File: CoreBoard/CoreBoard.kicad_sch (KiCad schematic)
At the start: 6 parts, among them J1 RJ45_LED_Shielded, U1 OKI, U2 Teensy4.1_DEV-16771

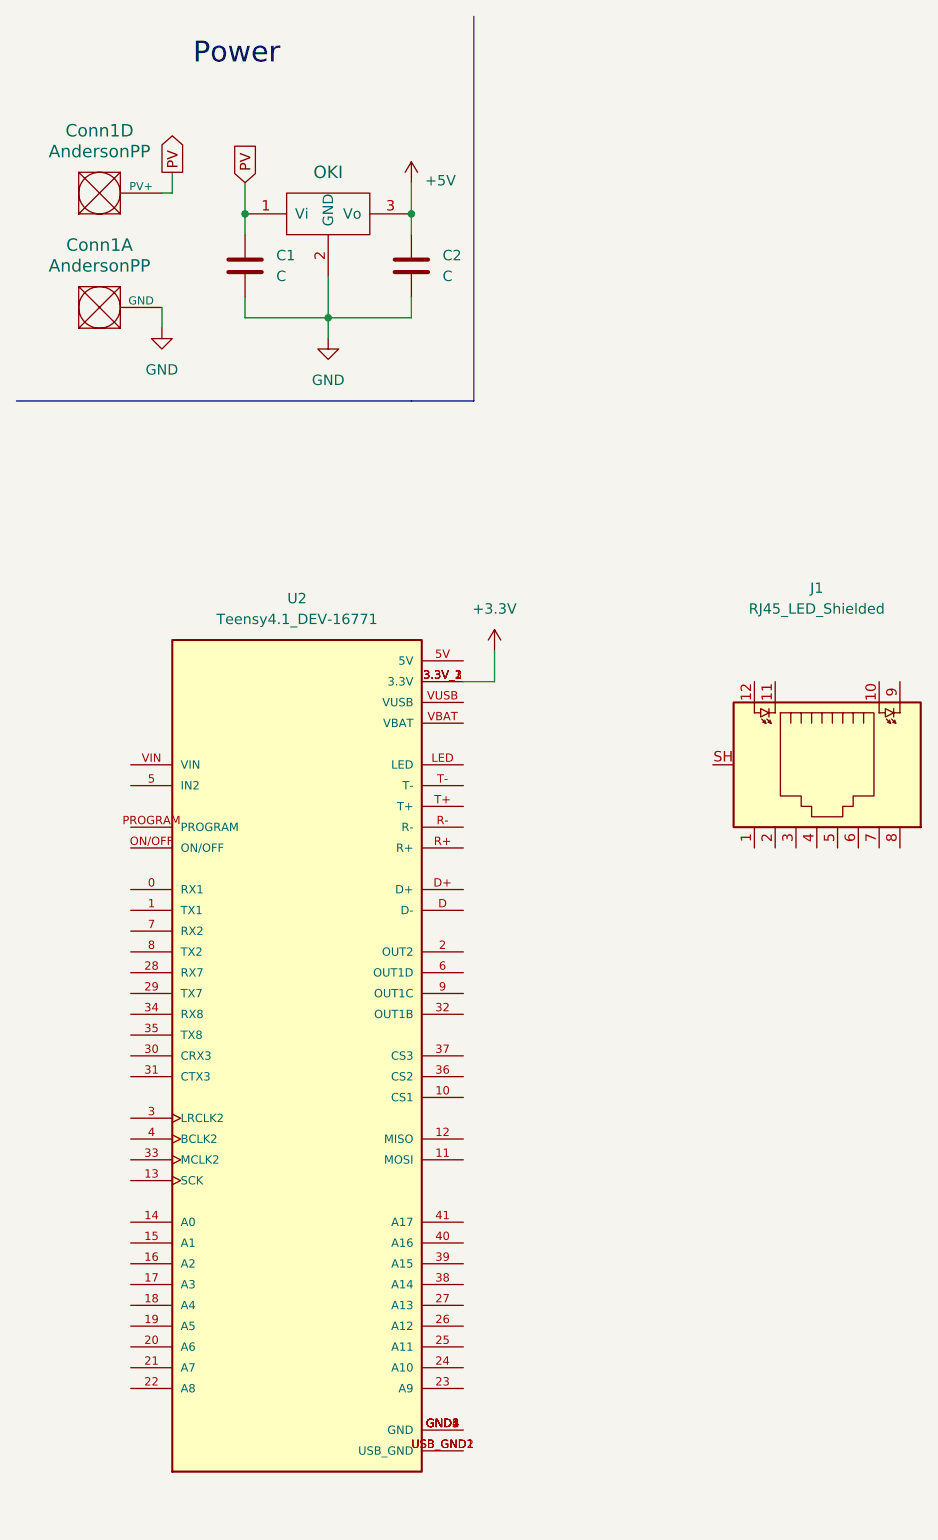
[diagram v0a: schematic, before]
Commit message: Added connections between the Teensy and the Ethernet Port, and the capacitance values were added for capacitors
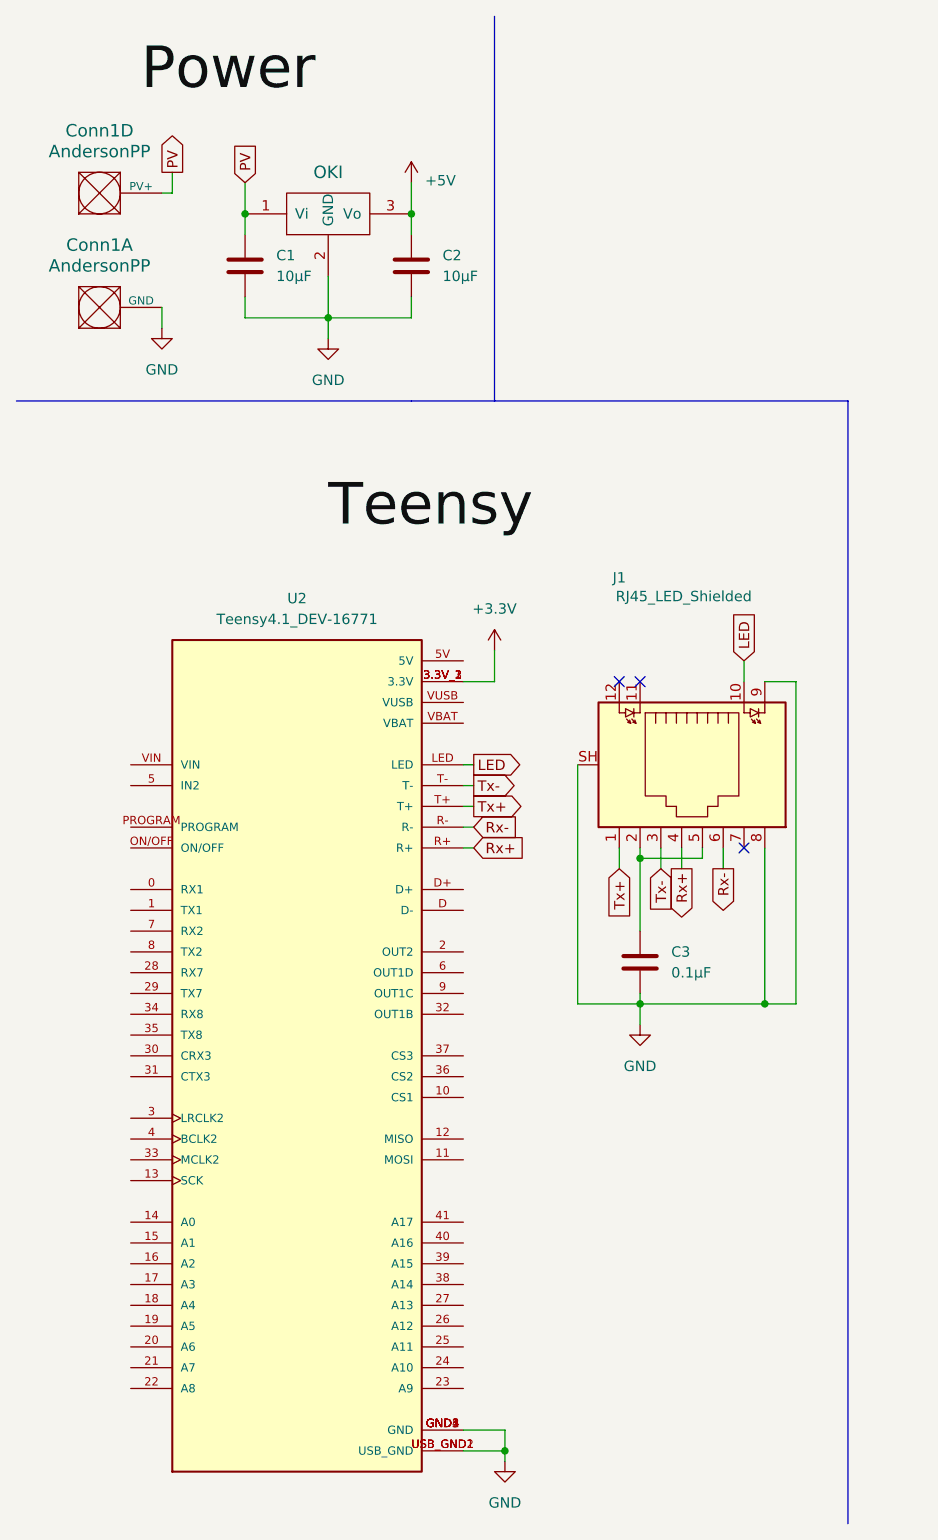
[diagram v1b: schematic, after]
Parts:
- added C3: 0.1µF, symbol Device:C
- C1, C2: value C -> 10µF
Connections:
- net GND: now also J1.8, J1.9, J1.SH, U2.GND1 (GND), U2.GND2 (GND), U2.GND3 (GND), U2.GND4 (GND), U2.GND5 (GND), U2.USB_GND1 (USB_GND), U2.USB_GND2 (USB_GND), C3.2
- net Tx+: now reaches J1.1
- net Tx+: now also U2.T+
- net LED: now reaches J1.10
- net LED: now also U2.LED
- net at J1.2: now also J1.5, C3.1
- net Tx-: now reaches J1.3
- net Tx-: now also U2.T-
- net Rx+: now reaches J1.4
- net Rx+: now also U2.R+
- net Rx-: now reaches J1.6
- net Rx-: now also U2.R-
- no-connect marks 0 -> 3
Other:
- moved on the sheet: J1

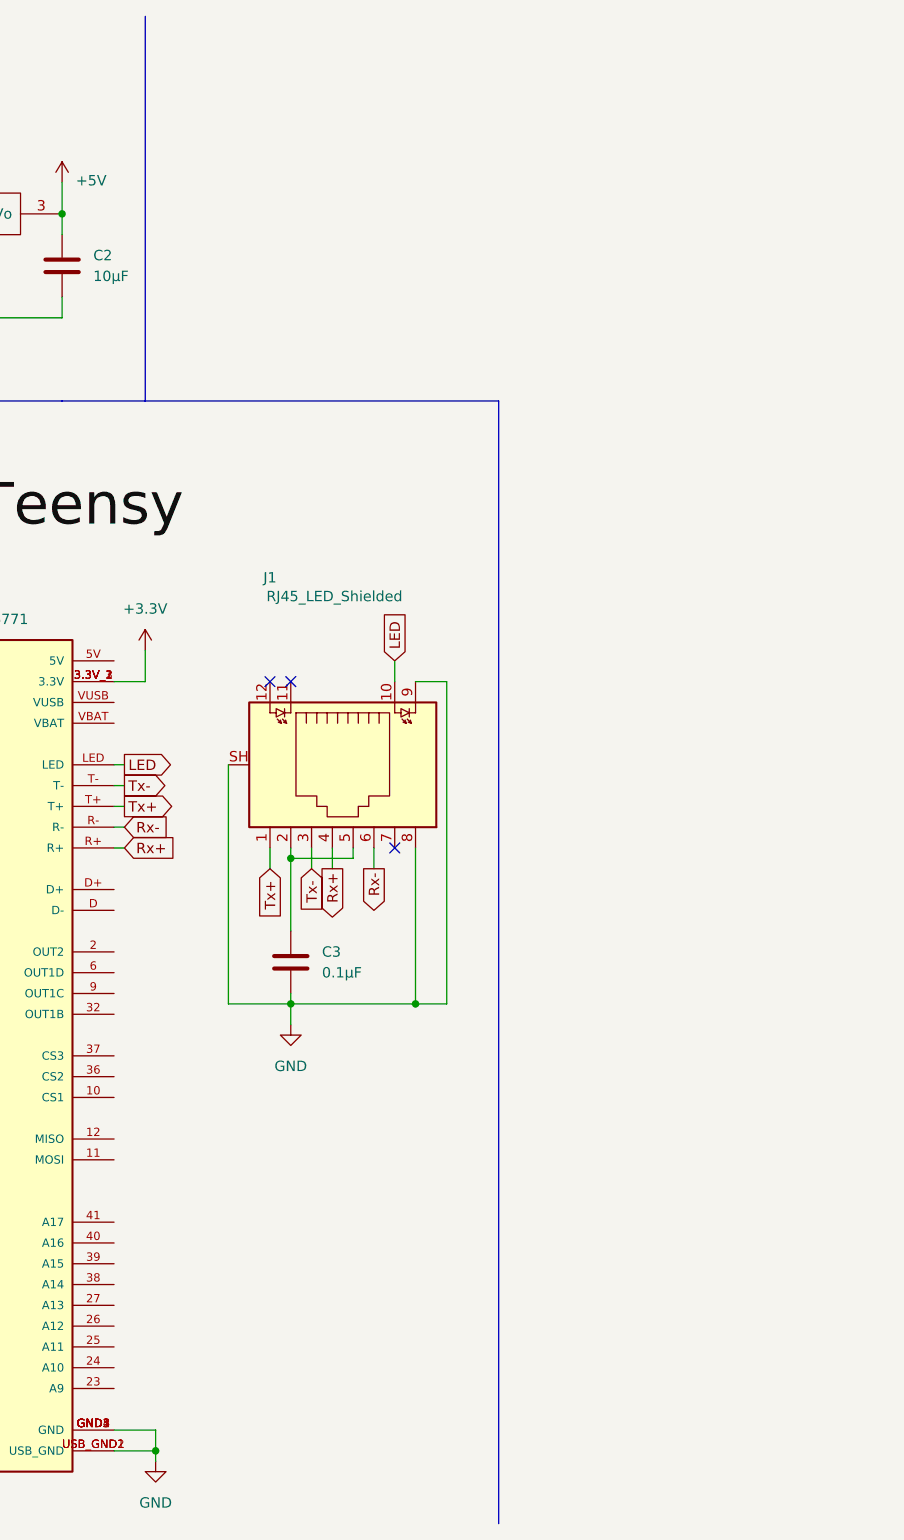
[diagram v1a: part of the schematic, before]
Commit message: Added Power LEDs and one button
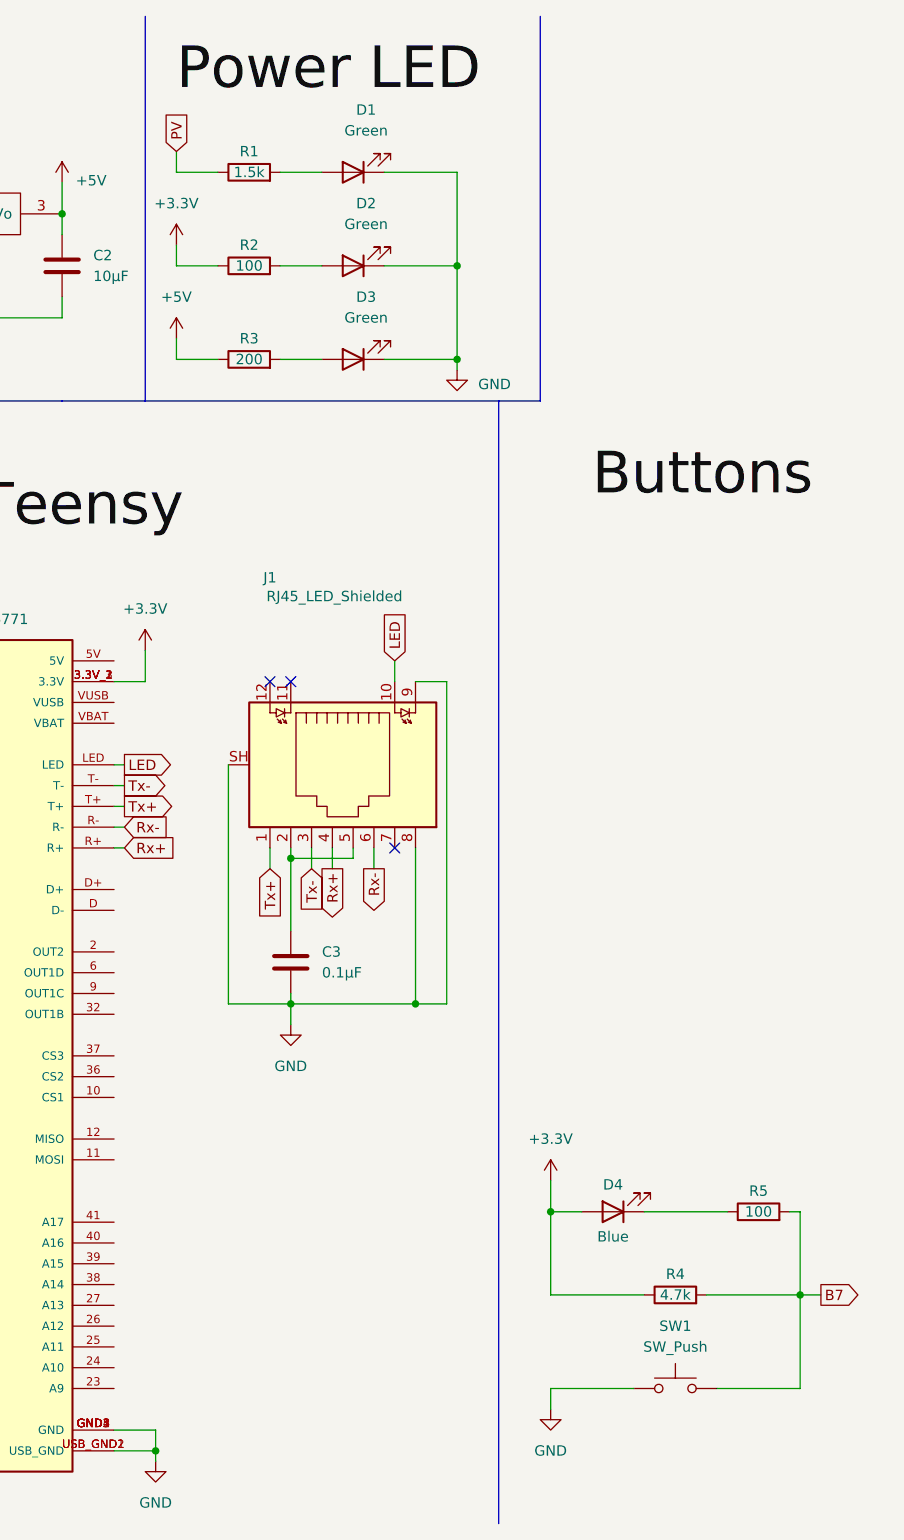
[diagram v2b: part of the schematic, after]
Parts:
- added D1, D2, D3: Green, symbol Device:LED
- added D4: Blue, symbol Device:LED
- added R1: 1.5k, symbol Device:R
- added R2, R5: 100, symbol Device:R
- added R3: 200, symbol Device:R
- added R4: 4.7k, symbol Device:R
- added SW1: SW_Push, symbol Switch:SW_Push
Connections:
- net +3.3V: now also D4.2 (A), R2.1, R4.1
- net +5V: now also R3.1
- net GND: now also D1.1 (K), D2.1 (K), D3.1 (K), SW1.1
- net PV: now also R1.1
- new net: D4.1 (K), R5.1
- new net: D1.2 (A), R1.2
- new net: D2.2 (A), R2.2
- new net: D3.2 (A), R3.2
- new net B7: R4.2, R5.2, SW1.2

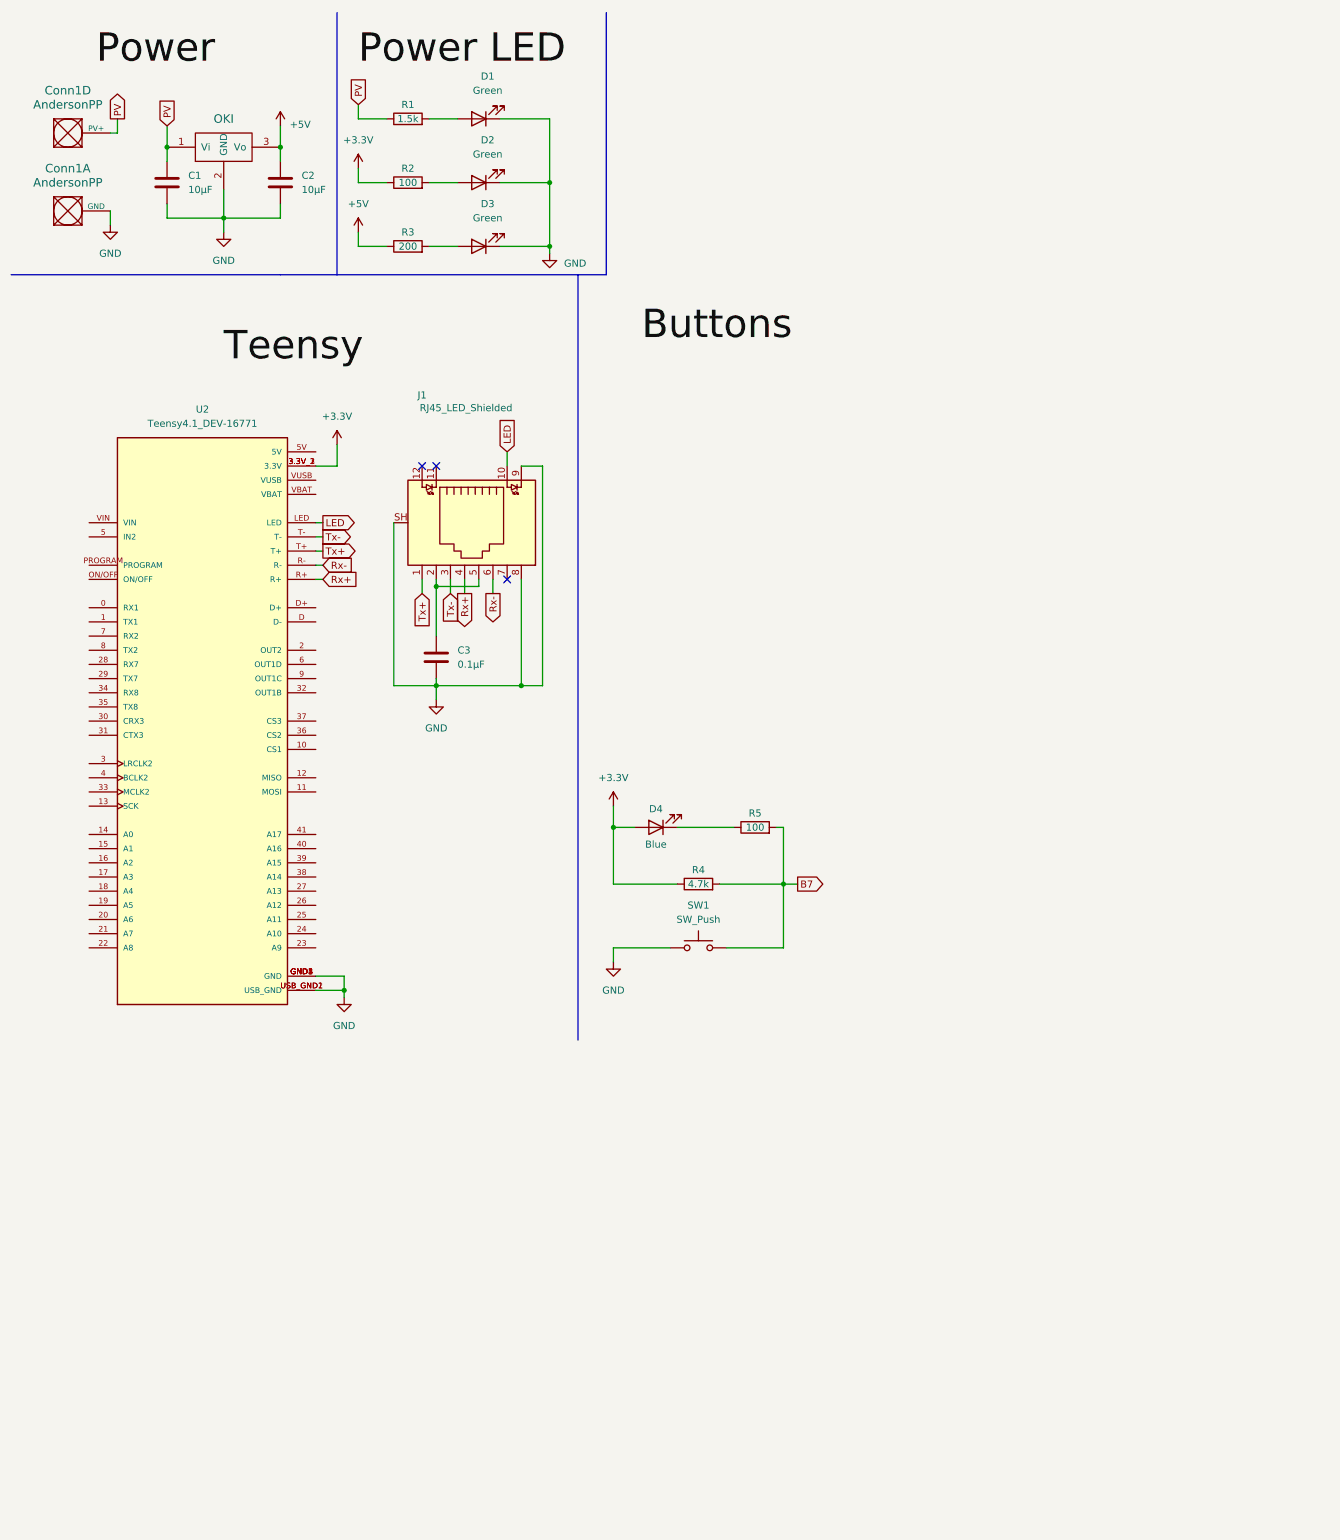
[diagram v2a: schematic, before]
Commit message: Increased the size of the schematic and added remaining buttons, resistor values for buttons may need to be redone
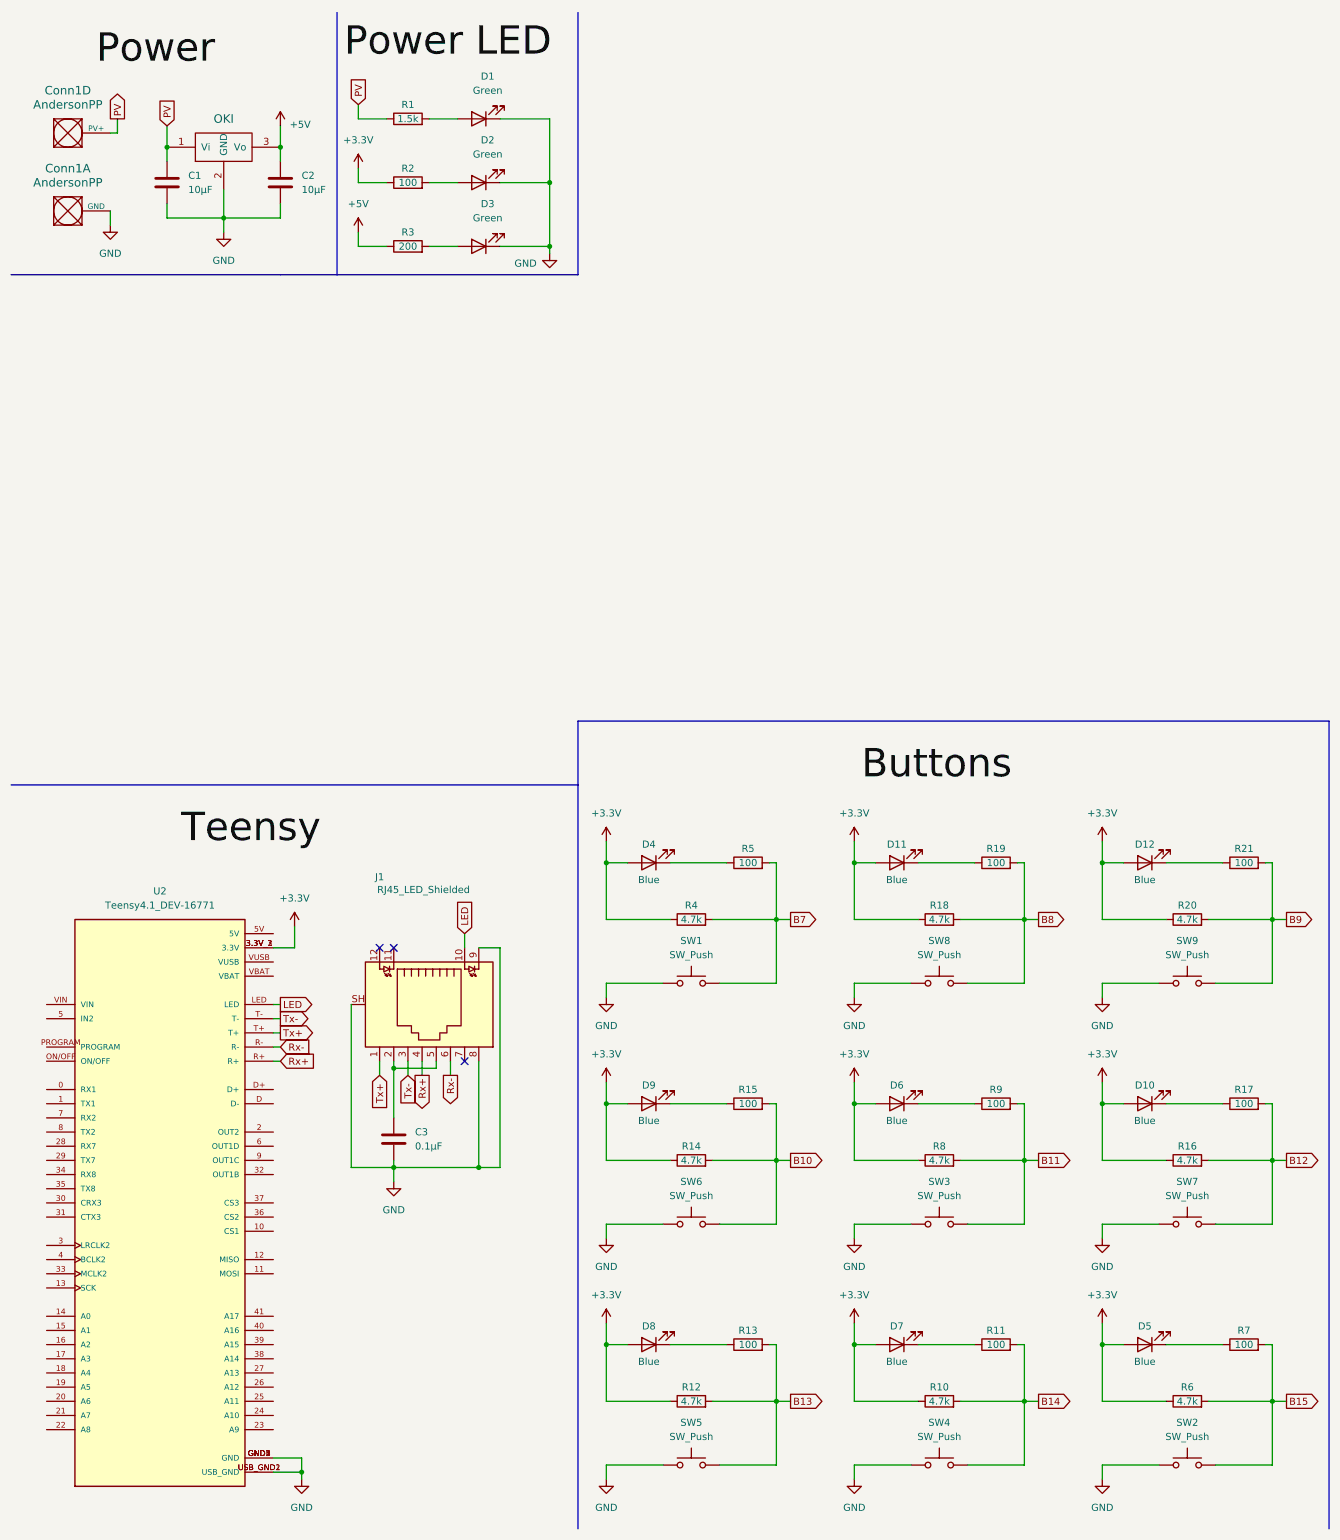
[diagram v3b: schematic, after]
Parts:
- added D10, D11, D12, D5, D6, D7, D8, D9: Blue, symbol Device:LED
- added R10, R12, R14, R16, R18, R20, R6, R8: 4.7k, symbol Device:R
- added R11, R13, R15, R17, R19, R21, R7, R9: 100, symbol Device:R
- added SW2, SW3, SW4, SW5, SW6, SW7, SW8, SW9: SW_Push, symbol Switch:SW_Push
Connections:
- net +3.3V: now also D10.2 (A), D11.2 (A), D12.2 (A), D5.2 (A), D6.2 (A), D7.2 (A), D8.2 (A), D9.2 (A), R10.1, R12.1, R14.1, R16.1, R18.1, R20.1, R6.1, R8.1
- net GND: now also SW2.1, SW3.1, SW4.1, SW5.1, SW6.1, SW7.1, SW8.1, SW9.1
- new net: D6.1 (K), R9.1
- new net: D12.1 (K), R21.1
- new net: D11.1 (K), R19.1
- new net: D9.1 (K), R15.1
- new net: D10.1 (K), R17.1
- new net: D8.1 (K), R13.1
- new net: D7.1 (K), R11.1
- new net: D5.1 (K), R7.1
- new net B10: R14.2, R15.2, SW6.2
- new net B11: R8.2, R9.2, SW3.2
- new net B12: R16.2, R17.2, SW7.2
- new net B13: R12.2, R13.2, SW5.2
- new net B14: R10.2, R11.2, SW4.2
- new net B15: R6.2, R7.2, SW2.2
- new net B8: R18.2, R19.2, SW8.2
- new net B9: R20.2, R21.2, SW9.2
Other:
- moved on the sheet: C3, J1, U2
